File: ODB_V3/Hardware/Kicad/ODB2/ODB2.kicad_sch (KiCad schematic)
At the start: 83 parts, among them U8 STM32F412ZGTx, Y1 ABM8G-25.000MHZ-18-D2Y-T

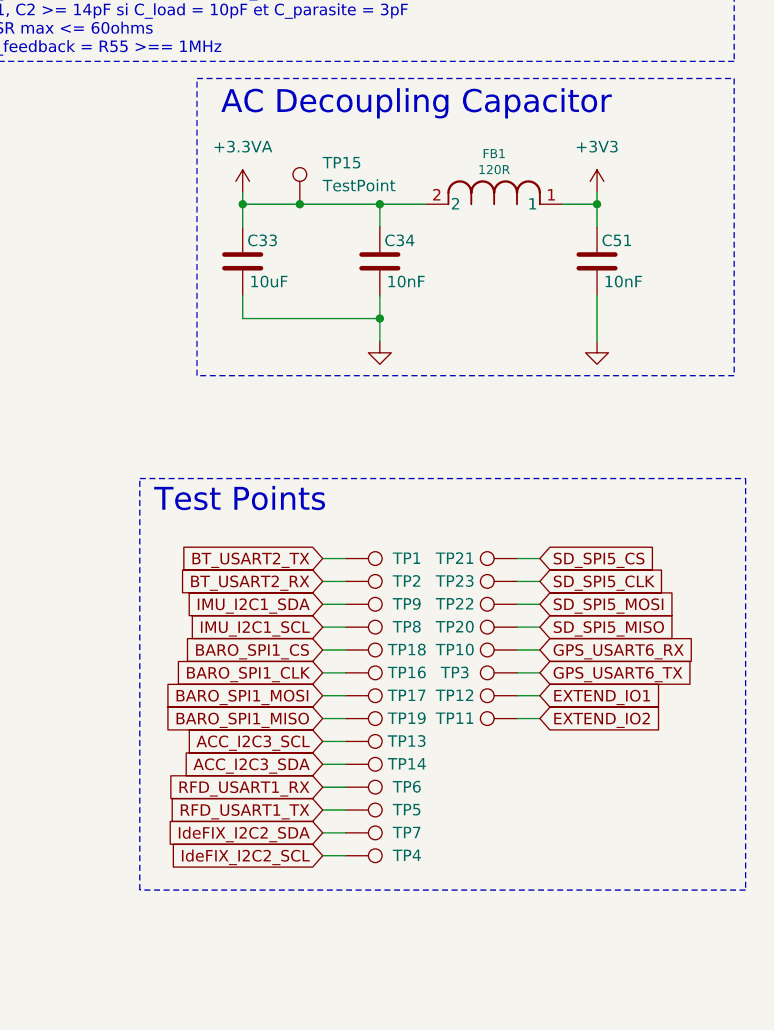
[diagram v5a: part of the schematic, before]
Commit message: fix : change components for order
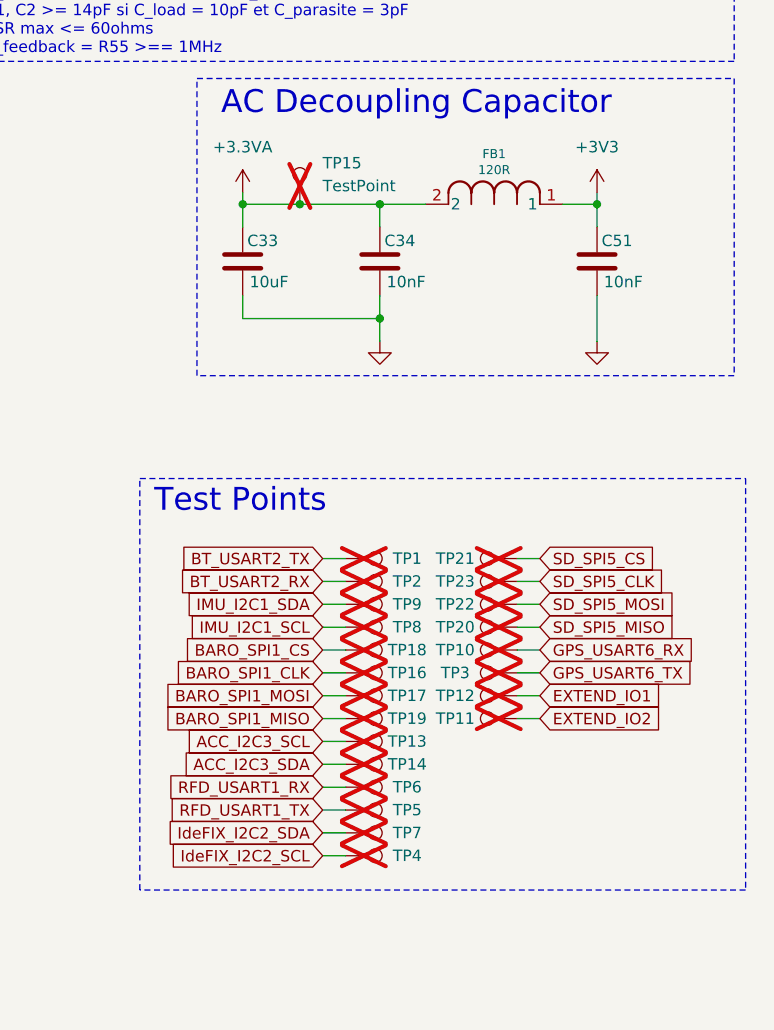
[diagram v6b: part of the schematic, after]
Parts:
- R10: DigiKey_Part_Number 408-1766-1-ND -> P1.5KDBCT-ND; Manufacturer_Part_Number URG1608L-152-L-T05 -> ERA-3AEB152V
- TP1, TP10, TP11, TP12, TP13, TP14, TP15, TP16, TP17, TP18, TP19, TP2, TP20, TP21, TP22, TP23, TP3, TP4, TP5, TP6, TP7, TP8, TP9: now not fitted
- Y1: DigiKey_Part_Number 535-10275-1-ND -> 535-14129-1-ND; Manufacturer_Part_Number ABM8G-25.000MHZ-18-D2Y-T -> ABM8G-25.000MHZ-18-D2Y-T3
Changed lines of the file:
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@@
 		(in_bom yes)
 		(on_board yes)
-		(dnp no)
+		(dnp yes)
 		(property "Reference" "TP16"
 			(at 368.808 227.33 90)
@@
 		(in_bom yes)
 		(on_board yes)
-		(dnp no)
+		(dnp yes)
 		(property "Reference" "TP19"
 			(at 368.808 232.41 90)
@@
 		(in_bom yes)
 		(on_board yes)
-		(dnp no)
+		(dnp yes)
 		(property "Reference" "TP13"
 			(at 368.808 234.95 90)
@@
 		(in_bom yes)
 		(on_board yes)
-		(dnp no)
+		(dnp yes)
 		(property "Reference" "TP22"
 			(at 374.142 219.71 90)
@@
 			)
 		)
-		(property "Datasheet" "https://www.digikey.ca/en/products/detail/susumu/URG1608L-152-L-T05/4552646"
+		(property "Datasheet" "https://www.digikey.ca/en/products/detail/panasonic-electronic-components/ERA-3AEB152V/1465858"
 			(at 382.27 31.75 0)
 			(effects
@@
 			)
 		)
-		(property "DigiKey_Part_Number" "408-1766-1-ND"
+		(property "DigiKey_Part_Number" "P1.5KDBCT-ND"
 			(at 382.27 31.75 90)
 			(effects
@@
 			)
 		)
-		(property "Manufacturer_Part_Number" "URG1608L-152-L-T05"
+		(property "Manufacturer_Part_Number" "ERA-3AEB152V"
 			(at 382.27 31.75 90)
 			(effects
@@
 		(in_bom yes)
 		(on_board yes)
-		(dnp no)
+		(dnp yes)
 		(property "Reference" "TP20"
 			(at 374.142 222.25 90)
@@
 		(in_bom yes)
 		(on_board yes)
-		(dnp no)
+		(dnp yes)
 		(property "Reference" "TP14"
 			(at 368.808 237.49 90)
@@
 		(in_bom yes)
 		(on_board yes)
-		(dnp no)
+		(dnp yes)
 		(property "Reference" "TP1"
 			(at 368.808 214.63 90)
@@
 		(in_bom yes)
 		(on_board yes)
-		(dnp no)
+		(dnp yes)
 		(property "Reference" "TP18"
 			(at 368.808 224.79 90)
@@
 		(in_bom yes)
 		(on_board yes)
-		(dnp no)
+		(dnp yes)
 		(property "Reference" "TP4"
 			(at 368.808 247.65 90)
@@
 		(in_bom yes)
 		(on_board yes)
-		(dnp no)
+		(dnp yes)
 		(property "Reference" "TP8"
 			(at 368.808 222.25 90)
@@
 		(in_bom yes)
 		(on_board yes)
-		(dnp no)
+		(dnp yes)
 		(fields_autoplaced yes)
 		(property "Reference" "TP15"
@@
 		(in_bom yes)
 		(on_board yes)
-		(dnp no)
+		(dnp yes)
 		(property "Reference" "TP11"
 			(at 374.142 232.41 90)
@@
 		(in_bom yes)
 		(on_board yes)
-		(dnp no)
+		(dnp yes)
 		(property "Reference" "TP6"
 			(at 368.808 240.03 90)
@@
 			)
 		)
-		(property "Datasheet" "https://www.digikey.ca/en/products/detail/abracon-llc/ABM8G-25-000MHZ-18-D2Y-T/2218021"
+		(property "Datasheet" "https://www.digikey.ca/en/products/detail/abracon-llc/ABM8G-25-000MHZ-18-D2Y-T3/2637895"
 			(at 340.36 132.08 0)
 			(effects
@@
 			)
 		)
-		(property "DigiKey_Part_Number" "535-10275-1-ND"
+		(property "DigiKey_Part_Number" "535-14129-1-ND"
 			(at 340.36 132.08 0)
 			(effects
@@
 			)
 		)
-		(property "Manufacturer_Part_Number" "ABM8G-25.000MHZ-18-D2Y-T"
+		(property "Manufacturer_Part_Number" "ABM8G-25.000MHZ-18-D2Y-T3"
 			(at 340.36 132.08 0)
 			(effects
@@
 		(in_bom yes)
 		(on_board yes)
-		(dnp no)
+		(dnp yes)
 		(property "Reference" "TP12"
 			(at 374.142 229.87 90)
@@
 		(in_bom yes)
 		(on_board yes)
-		(dnp no)
+		(dnp yes)
 		(property "Reference" "TP5"
 			(at 368.808 242.57 90)
@@
 		(in_bom yes)
 		(on_board yes)
-		(dnp no)
+		(dnp yes)
 		(property "Reference" "TP17"
 			(at 368.808 229.87 90)
@@
 		(in_bom yes)
 		(on_board yes)
-		(dnp no)
+		(dnp yes)
 		(property "Reference" "TP23"
 			(at 374.142 217.17 90)
@@
 		(in_bom yes)
 		(on_board yes)
-		(dnp no)
+		(dnp yes)
 		(property "Reference" "TP7"
 			(at 368.808 245.11 90)
@@
 		(in_bom yes)
 		(on_board yes)
-		(dnp no)
+		(dnp yes)
 		(property "Reference" "TP3"
 			(at 374.142 227.33 90)
@@
 		(in_bom yes)
 		(on_board yes)
-		(dnp no)
+		(dnp yes)
 		(property "Reference" "TP2"
 			(at 368.808 217.17 90)
@@
 		(in_bom yes)
 		(on_board yes)
-		(dnp no)
+		(dnp yes)
 		(property "Reference" "TP9"
 			(at 368.808 219.71 90)
@@
 		(in_bom yes)
 		(on_board yes)
-		(dnp no)
+		(dnp yes)
 		(property "Reference" "TP21"
 			(at 374.142 214.63 90)
@@
 		(in_bom yes)
 		(on_board yes)
-		(dnp no)
+		(dnp yes)
 		(property "Reference" "TP10"
 			(at 374.142 224.79 90)

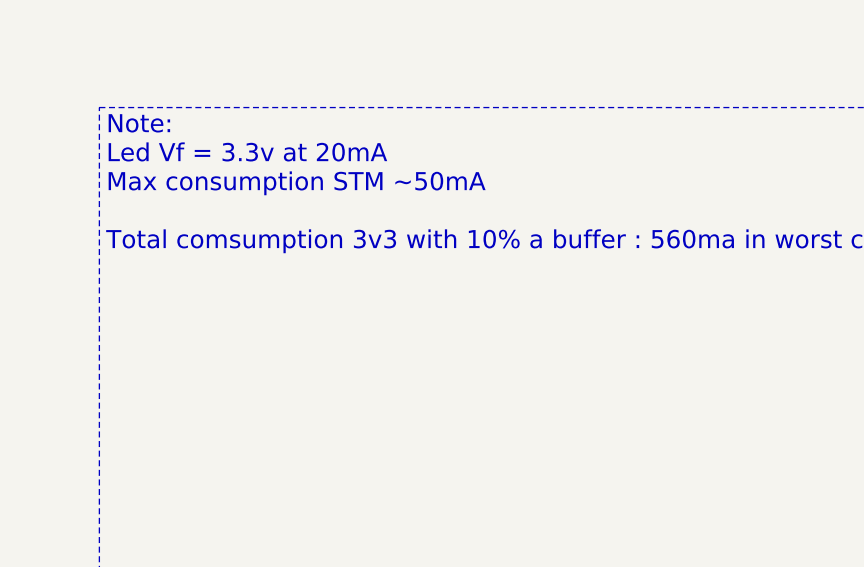
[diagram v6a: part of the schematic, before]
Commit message: new: create power debugger project + ad revision for consumption for ODBlix
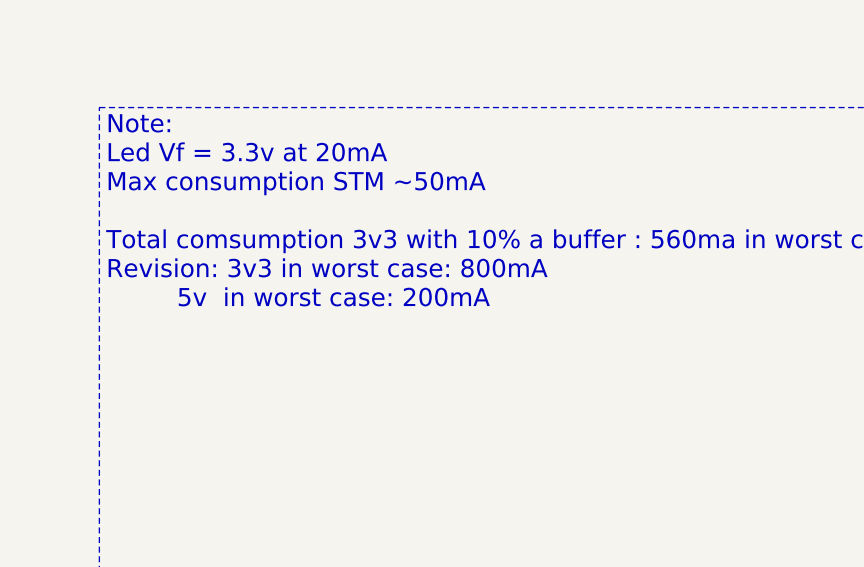
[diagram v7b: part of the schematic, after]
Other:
- note added: "Note: Led Vf = 3.3v at 20mA Max consumption STM ~50mA Total comsumption 3v3 with 10% a buffer : 560ma in worst case Revision: 3v3 in worst case: 800mA 5v in worst case: 200mA"
- note removed: "Note: Led Vf = 3.3v at 20mA Max consumption STM ~50mA Total comsumption 3v3 with 10% a buffer : 560ma in worst case"
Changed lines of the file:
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@@
 		)
 	)
-	(text "Note:\nLed Vf = 3.3v at 20mA\nMax consumption STM ~50mA\n\nTotal comsumption 3v3 with 10% a buffer : 560ma in worst case"
+	(text "Note:\nLed Vf = 3.3v at 20mA\nMax consumption STM ~50mA\n\nTotal comsumption 3v3 with 10% a buffer : 560ma in worst case\nRevision: 3v3 in worst case: 800mA\n	     5v  in worst case: 200mA"
 		(exclude_from_sim no)
 		(at 14.732 225.044 0)

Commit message: chore: add power comsumption list
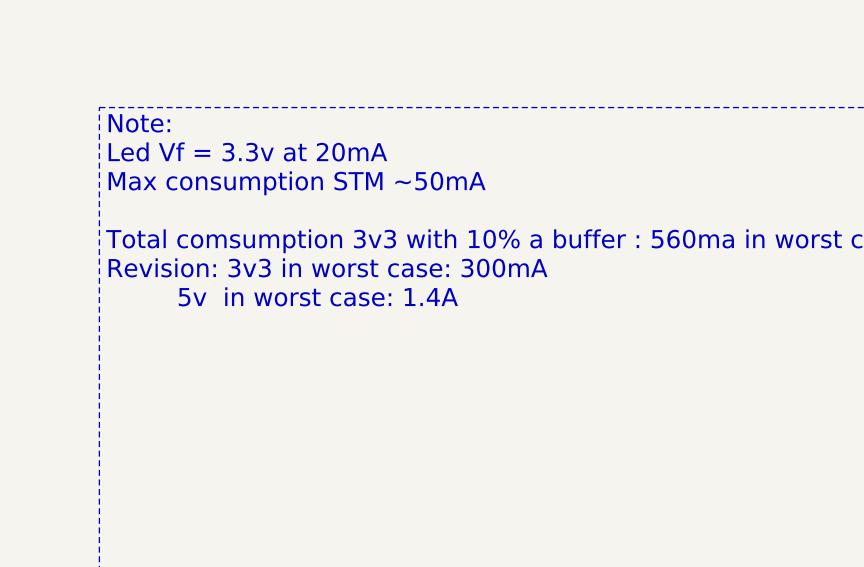
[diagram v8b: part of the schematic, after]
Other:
- note added: "Note: Led Vf = 3.3v at 20mA Max consumption STM ~50mA Total comsumption 3v3 with 10% a buffer : 560ma in worst case Revision: 3v3 in worst case: 300mA 5v in worst case: 1.4A"
- note removed: "Note: Led Vf = 3.3v at 20mA Max consumption STM ~50mA Total comsumption 3v3 with 10% a buffer : 560ma in worst case Revision: 3v3 in worst case: 800mA 5v in worst case: 200mA"
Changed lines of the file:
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@@
 		)
 	)
-	(text "Note:\nLed Vf = 3.3v at 20mA\nMax consumption STM ~50mA\n\nTotal comsumption 3v3 with 10% a buffer : 560ma in worst case\nRevision: 3v3 in worst case: 800mA\n	     5v  in worst case: 200mA"
+	(text "Note:\nLed Vf = 3.3v at 20mA\nMax consumption STM ~50mA\n\nTotal comsumption 3v3 with 10% a buffer : 560ma in worst case\nRevision: 3v3 in worst case: 300mA\n	     5v  in worst case: 1.4A"
 		(exclude_from_sim no)
 		(at 14.732 225.044 0)
